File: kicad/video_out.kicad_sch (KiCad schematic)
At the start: 39 parts, among them J6 3.5 mm, J7 VGA, U16 ATF22V10C-10PU, U22 SN74F377AN, U23 SN74F377AN, U36 SN74HCT574N

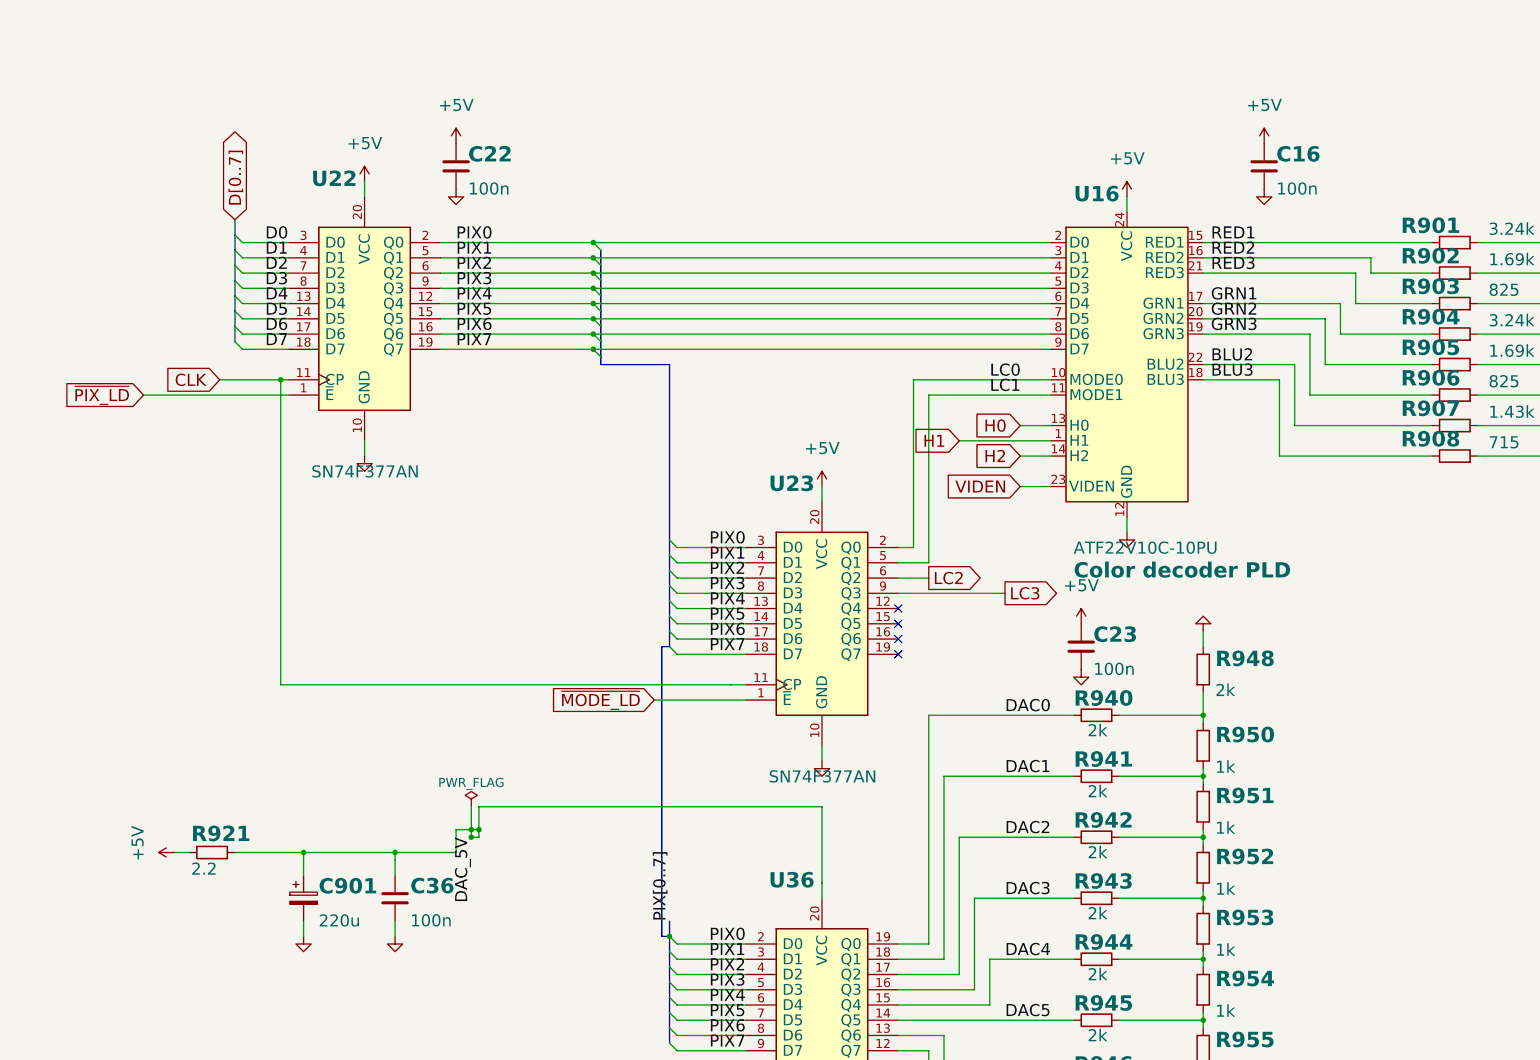
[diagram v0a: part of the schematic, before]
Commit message: Tidy every schematic sheet: spread parts, straight runs, buses kept, horizontal tabs
Shared port, expansion and cartridge sheets laid out by hand; buses from
other sheets get a bus label at each chip, busy control nets a label at
each pin; some PLD and connector symbols reordered so wires run straight;
sideways power symbols read across. 0 netlist problems, no overlaps.

Co-Authored-By: Claude Opus 5.5 (1M context) <noreply@anthropic.com>
Claude-Session: https://claude.ai/code/session_01L9AkLuEg13EebxDmgXsaEp
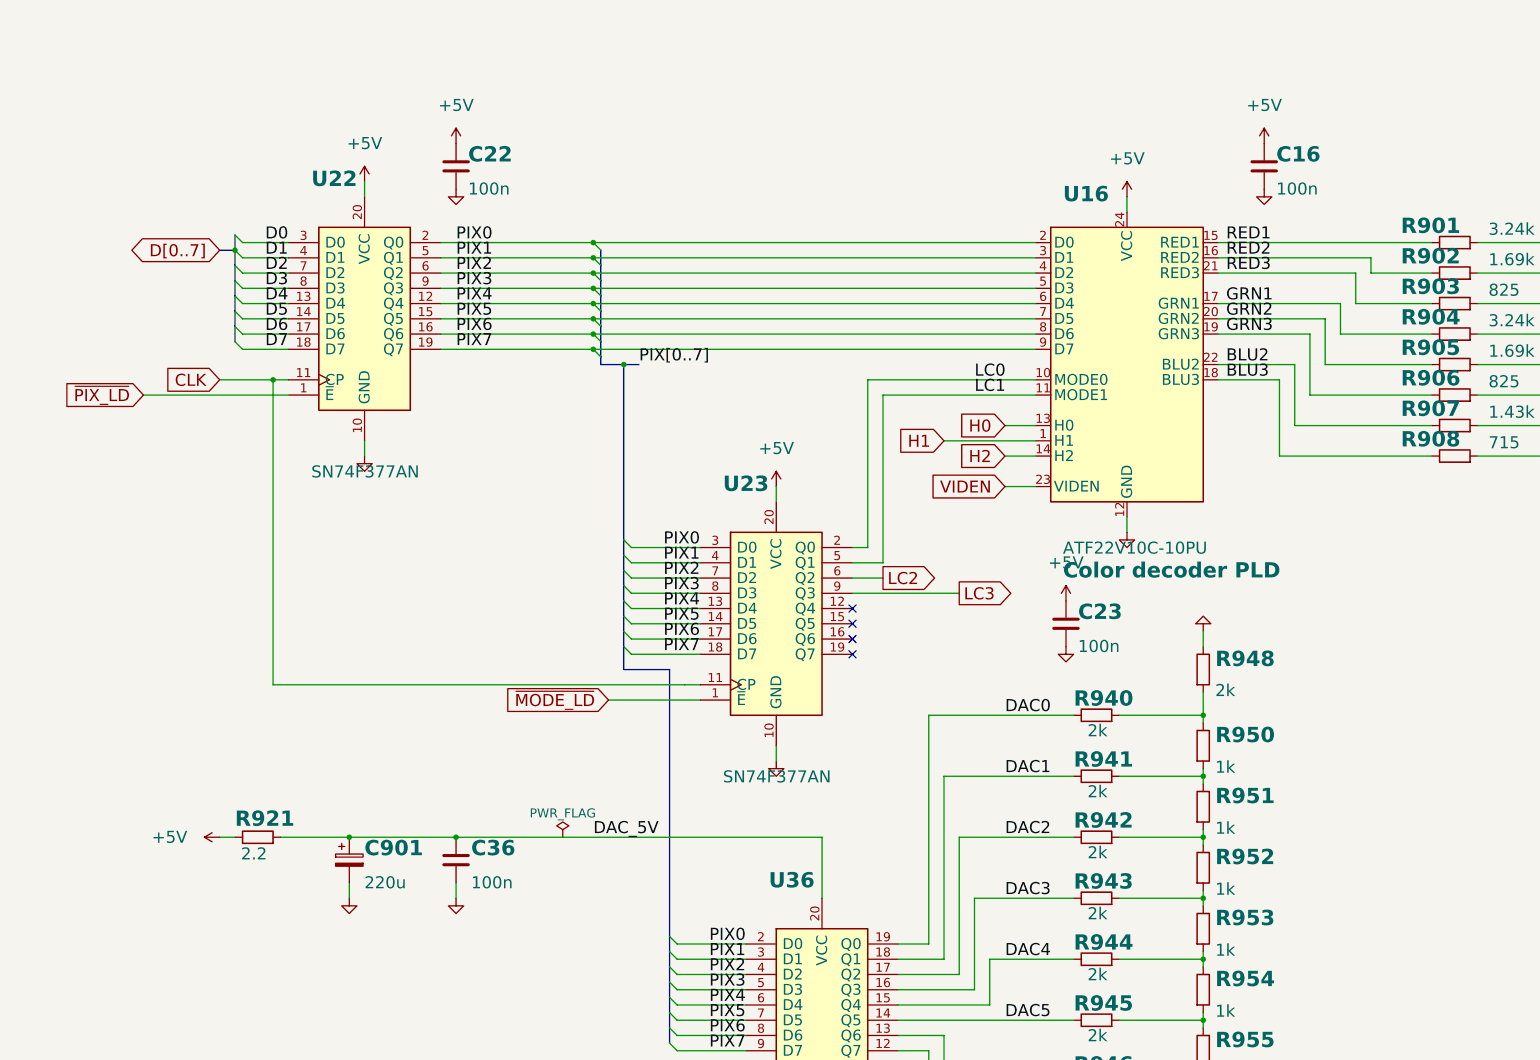
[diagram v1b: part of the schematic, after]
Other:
- moved on the sheet: C23, C36, C901, R921, U23

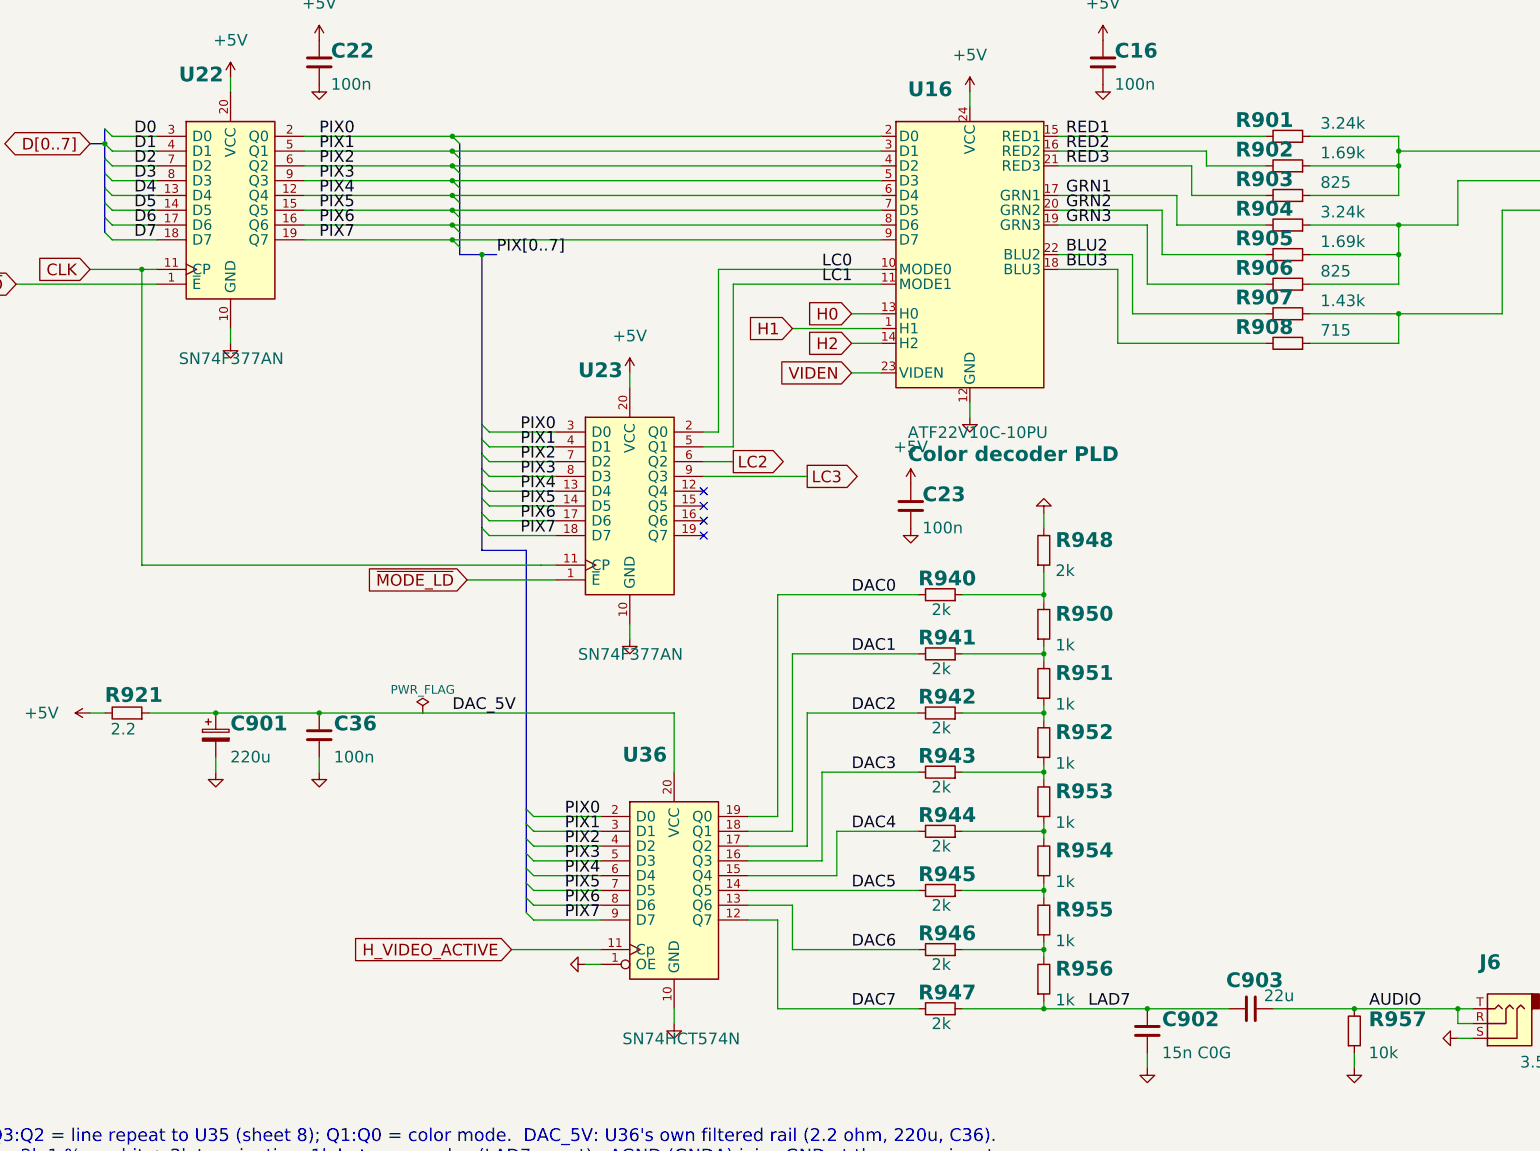
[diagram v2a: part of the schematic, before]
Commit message: Number parts from 1 for each kind; US zigzag resistor symbols
Main board R1-R54, RN1-RN2, D1-D5, JP1-JP2, F1, NT1, non-decoupling
capacitors C41-C46 (decaps keep Cn = Un); keyboard keys 1-63 row by row
(SWn, Dn, Rn per key). Resistors use R_US / R_Network08_US. --check now
fails on gaps or hundreds in the numbering. PDFs regenerated.

Co-Authored-By: Claude Opus 5.5 (1M context) <noreply@anthropic.com>
Claude-Session: https://claude.ai/code/session_01L9AkLuEg13EebxDmgXsaEp
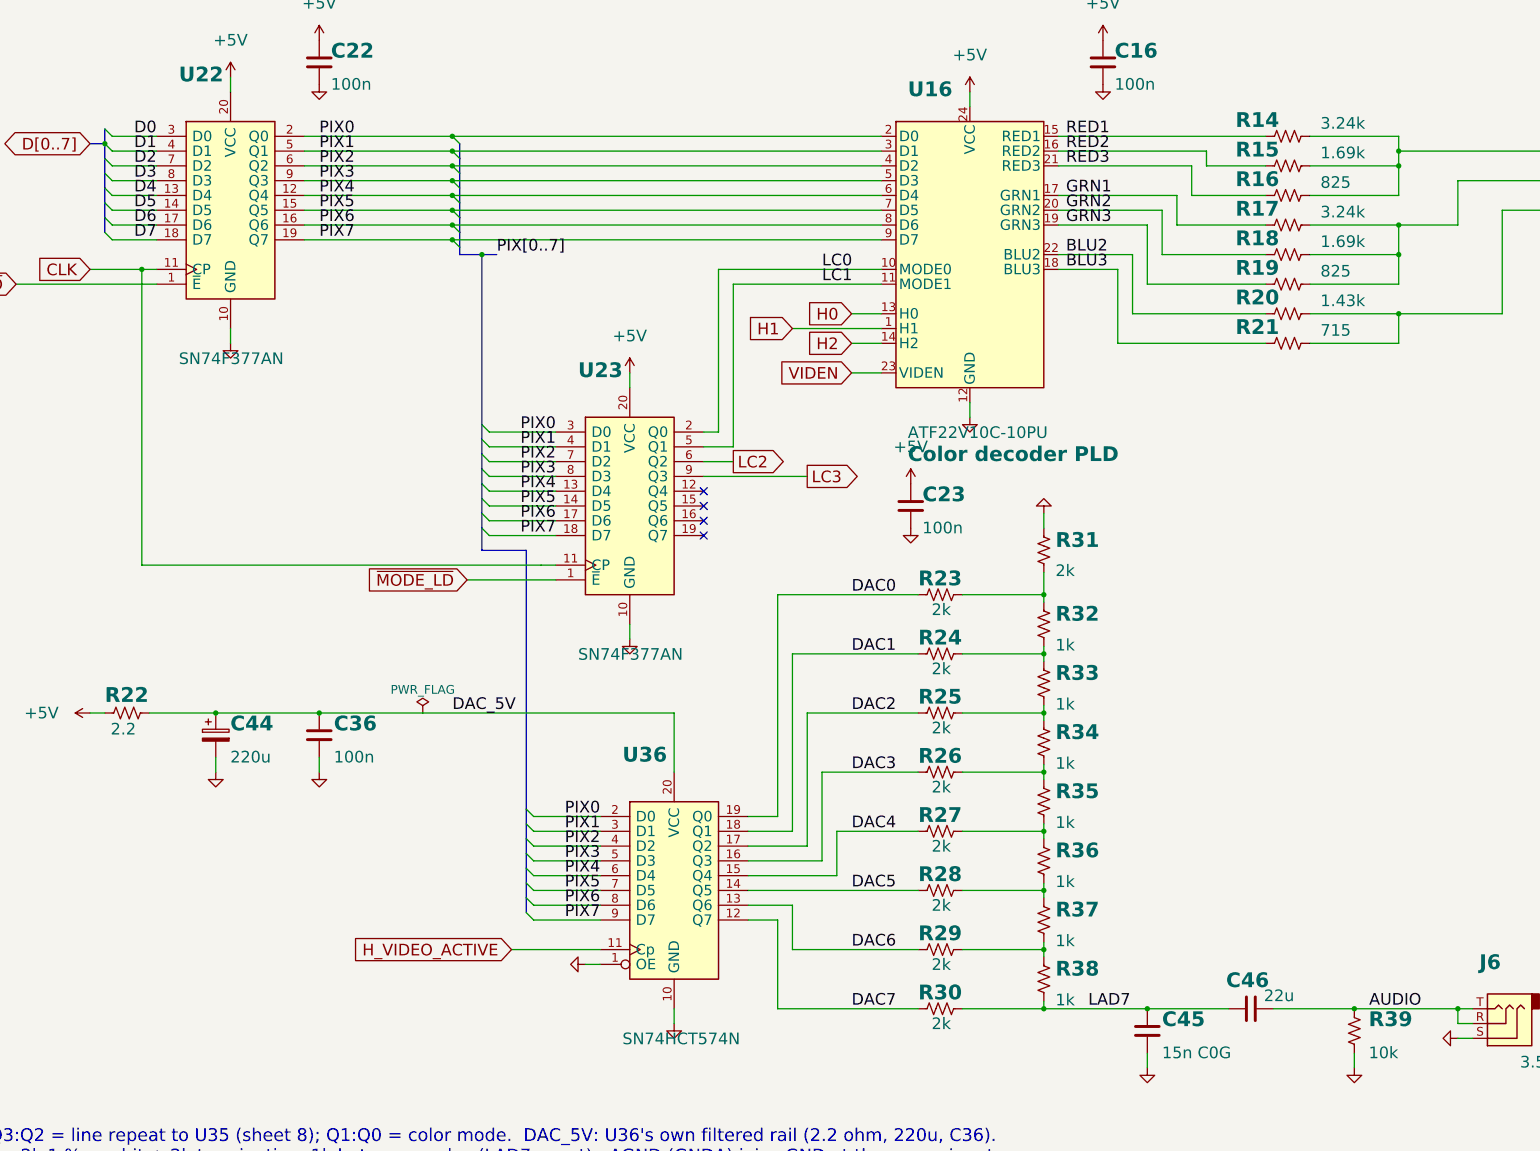
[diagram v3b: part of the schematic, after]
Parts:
- removed C901: 220u, Capacitor_THT:CP_Radial_D6.3mm_P2.50mm, symbol placard_std:C_Polarized
- removed C902: 15n C0G, Capacitor_THT:C_Disc_D5.0mm_W2.5mm_P5.00mm, symbol placard_std:C
- removed C903: 22u, Capacitor_THT:C_Disc_D5.0mm_W2.5mm_P5.00mm, symbol placard_std:C
- removed R901, R904: 3.24k, Resistor_THT:R_Axial_DIN0207_L6.3mm_D2.5mm_P10.16mm_Horizontal, symbol placard_std:R
- removed R902, R905: 1.69k, Resistor_THT:R_Axial_DIN0207_L6.3mm_D2.5mm_P10.16mm_Horizontal, symbol placard_std:R
- removed R903, R906: 825, Resistor_THT:R_Axial_DIN0207_L6.3mm_D2.5mm_P10.16mm_Horizontal, symbol placard_std:R
- removed R907: 1.43k, Resistor_THT:R_Axial_DIN0207_L6.3mm_D2.5mm_P10.16mm_Horizontal, symbol placard_std:R
- removed R908: 715, Resistor_THT:R_Axial_DIN0207_L6.3mm_D2.5mm_P10.16mm_Horizontal, symbol placard_std:R
- removed R921: 2.2, Resistor_THT:R_Axial_DIN0207_L6.3mm_D2.5mm_P10.16mm_Horizontal, symbol placard_std:R
- removed R940, R941, R942, R943, R944, R945, R946, R947, R948: 2k, Resistor_THT:R_Axial_DIN0207_L6.3mm_D2.5mm_P10.16mm_Horizontal, symbol placard_std:R
- removed R950, R951, R952, R953, R954, R955, R956: 1k, Resistor_THT:R_Axial_DIN0207_L6.3mm_D2.5mm_P10.16mm_Horizontal, symbol placard_std:R
- removed R957: 10k, Resistor_THT:R_Axial_DIN0207_L6.3mm_D2.5mm_P10.16mm_Horizontal, symbol placard_std:R
- added C44: 220u, Capacitor_THT:CP_Radial_D6.3mm_P2.50mm, symbol placard_std:C_Polarized
- added C45: 15n C0G, Capacitor_THT:C_Disc_D5.0mm_W2.5mm_P5.00mm, symbol placard_std:C
- added C46: 22u, Capacitor_THT:C_Disc_D5.0mm_W2.5mm_P5.00mm, symbol placard_std:C
- added R14, R17: 3.24k, Resistor_THT:R_Axial_DIN0207_L6.3mm_D2.5mm_P10.16mm_Horizontal, symbol placard_std:R_US
- added R15, R18: 1.69k, Resistor_THT:R_Axial_DIN0207_L6.3mm_D2.5mm_P10.16mm_Horizontal, symbol placard_std:R_US
- added R16, R19: 825, Resistor_THT:R_Axial_DIN0207_L6.3mm_D2.5mm_P10.16mm_Horizontal, symbol placard_std:R_US
- added R20: 1.43k, Resistor_THT:R_Axial_DIN0207_L6.3mm_D2.5mm_P10.16mm_Horizontal, symbol placard_std:R_US
- added R21: 715, Resistor_THT:R_Axial_DIN0207_L6.3mm_D2.5mm_P10.16mm_Horizontal, symbol placard_std:R_US
- added R22: 2.2, Resistor_THT:R_Axial_DIN0207_L6.3mm_D2.5mm_P10.16mm_Horizontal, symbol placard_std:R_US
- added R23, R24, R25, R26, R27, R28, R29, R30, R31: 2k, Resistor_THT:R_Axial_DIN0207_L6.3mm_D2.5mm_P10.16mm_Horizontal, symbol placard_std:R_US
- added R32, R33, R34, R35, R36, R37, R38: 1k, Resistor_THT:R_Axial_DIN0207_L6.3mm_D2.5mm_P10.16mm_Horizontal, symbol placard_std:R_US
- added R39: 10k, Resistor_THT:R_Axial_DIN0207_L6.3mm_D2.5mm_P10.16mm_Horizontal, symbol placard_std:R_US
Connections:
- net +5V: now also R22.1
- net AUDIO: now also C46.2, R39.1
- net BLU2: now also R20.1
- net BLU3: now also R21.1
- net DAC0: now also R23.1
- net DAC1: now also R24.1
- net DAC2: now also R25.1
- net DAC3: now also R26.1
- net DAC4: now also R27.1
- net DAC5: now also R28.1
- net DAC6: now also R29.1
- net DAC7: now also R30.1
- net DAC_5V: now also C44.1, R22.2
- net GNDA: now also C44.2, C45.2, R31.1, R39.2
- net GRN1: now also R17.1
- net GRN2: now also R18.1
- net GRN3: now also R19.1
- net LAD7: now also C45.1, C46.1, R30.2, R38.2
- net RED1: now also R14.1
- net RED2: now also R15.1
- net RED3: now also R16.1
- net VGA_B: now also R20.2, R21.2
- net VGA_G: now also R17.2, R18.2, R19.2
- net VGA_R: now also R14.2, R15.2, R16.2
- new net: R29.2, R37.2, R38.1
- new net: R26.2, R34.2, R35.1
- new net: R27.2, R35.2, R36.1
- new net: R28.2, R36.2, R37.1
- new net: R25.2, R33.2, R34.1
- new net: R23.2, R31.2, R32.1
- new net: R24.2, R32.2, R33.1

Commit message: Bill of materials for the main board, cartridge and keyboard
Manufacturer and MPN fields on every schematic part (empty where none is
chosen), set from an MPN table in gen_kicad_schematic.py; net tie, cartridge
edge fingers and solder jumper excluded from the BOM.  gen_bom.py groups the
parts by part number into docs/BOM.md and docs/BOM.csv, adding sockets,
shunts, keyboard LEDs, keycaps, stabilizers and the keyboard ribbon cable.

Co-Authored-By: Claude Opus 5.5 (1M context) <noreply@anthropic.com>
Claude-Session: https://claude.ai/code/session_018iEnPngycbxX6Tt4Wzp3zN
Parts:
- U16: MPN (none) -> ATF22V10C-10PU; Manufacturer (none) -> Microchip
- U22, U23: MPN (none) -> SN74F377AN; Manufacturer (none) -> Texas Instruments
- U36: MPN (none) -> SN74HCT574N; Manufacturer (none) -> Texas Instruments
